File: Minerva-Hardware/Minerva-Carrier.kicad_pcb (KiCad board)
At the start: 4 copper layers, 83.5 x 90 mm, 75 parts, among them J1 HDMI_D_1.4, J11 USB_C_Receptacle_USB2.0, J14 JST_SHBM04B-SRSS-TB, J16 Conn_01x22_Female, J2 Conn_02x07_Odd_Even, J3 Bus_M.2_Socket_B, J4 Bus_M.2_Socket_M, J5 Conn_01x22_Female, J6 THD-02-R, J7 JAE_SIM_Card_SF72S006, J8 THD-20-R, SW1 Right angle Tact button, U1 BQ25798, U2 ASEK-32.768KHZ-L-R-T, U6 AP22653W6, U8 AP3441SHE-7B

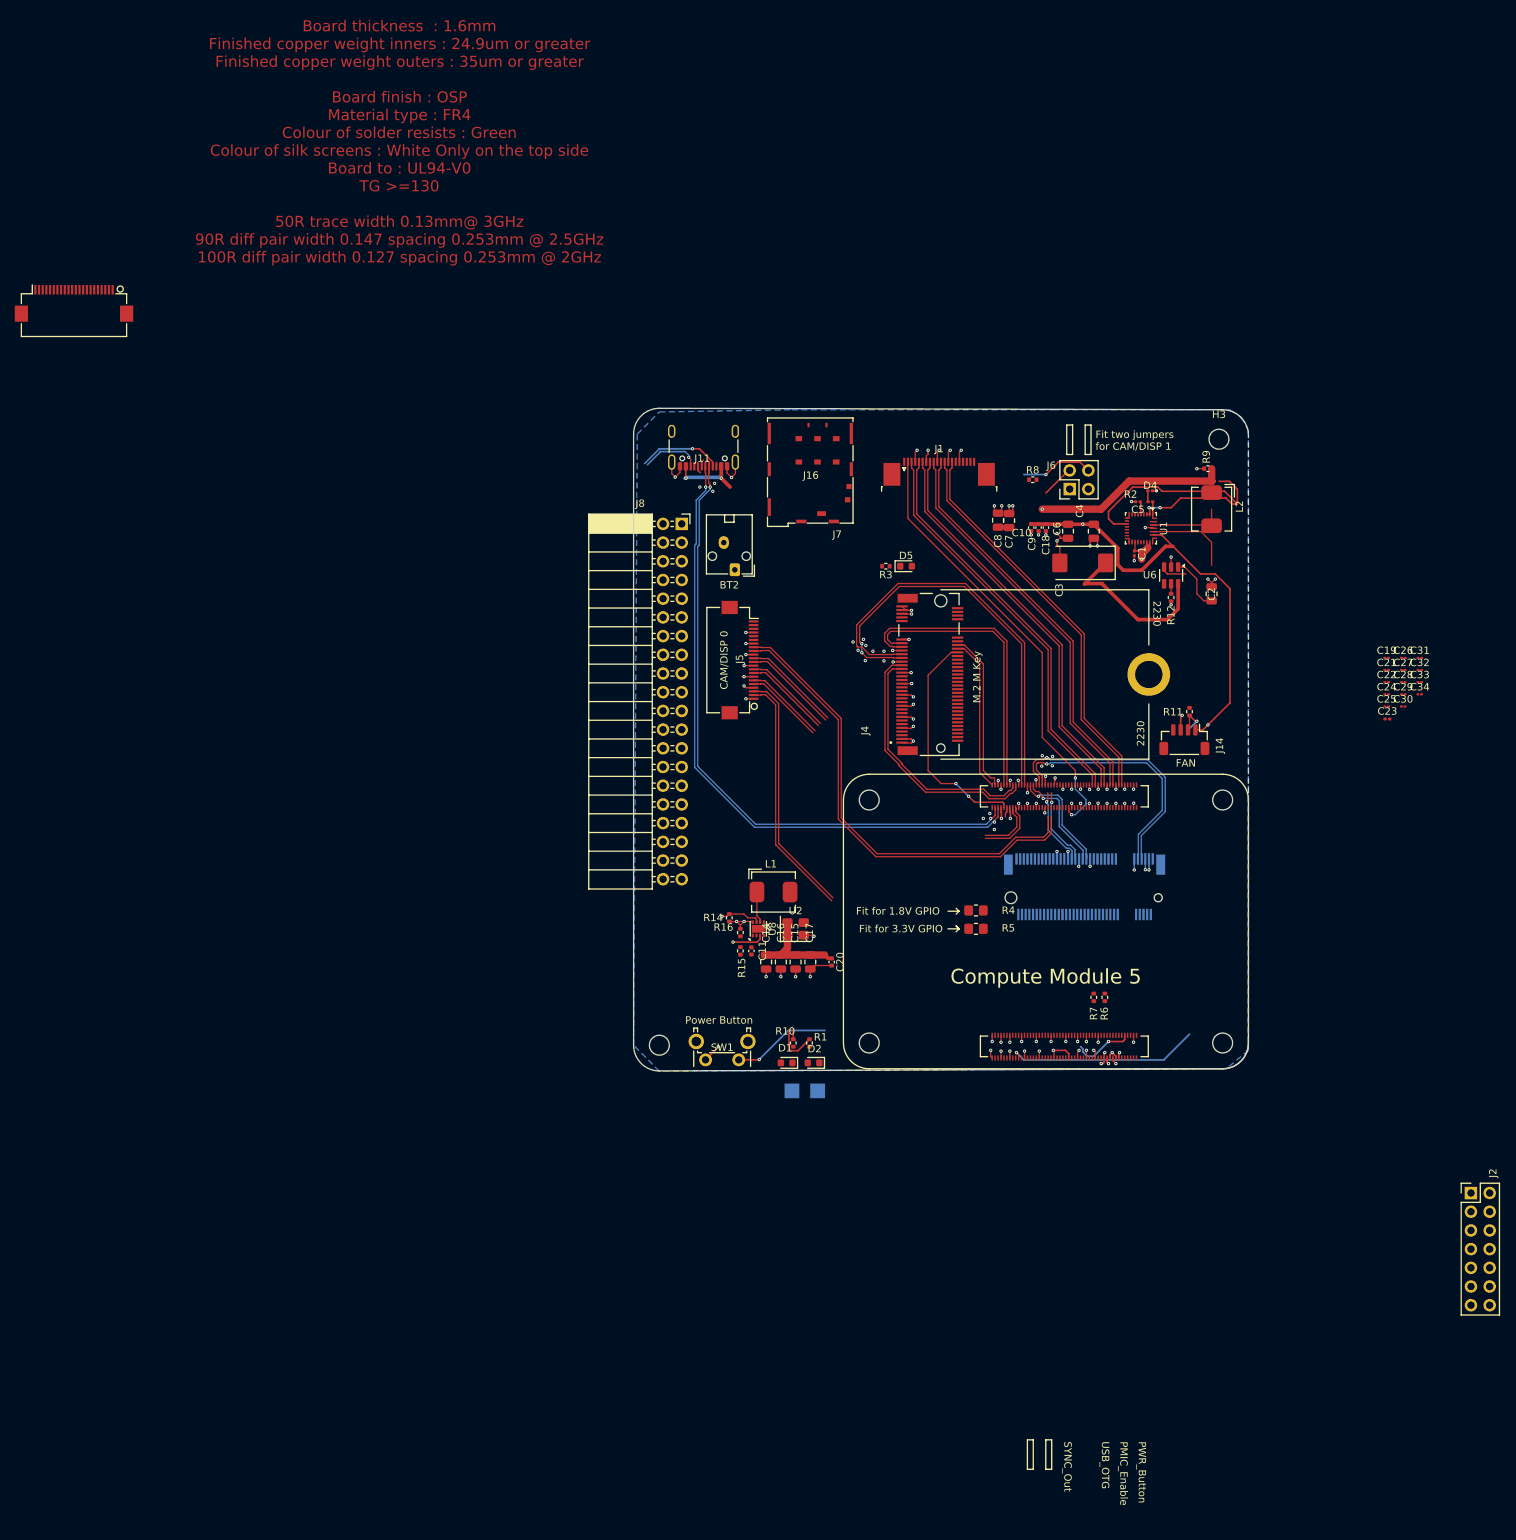
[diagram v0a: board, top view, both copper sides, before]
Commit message: Capture pre-existing Minerva hardware and Torchform work
Hardware schematics and power architecture
- Update carrier, CM5 GPIO, high-speed, PCIe/M.2, face-board, and root schematic hierarchy.
- Add USB-C/DisplayPort dock path, PD controller support, display bridge, audio amplifier, battery charging, boost conversion, fuel gauge, RTC backup, and MCU interconnect changes.
- Add the relocated power/USB schematic and associated local symbols, footprints, and 3D models.

PCB and design assets
- Update the carrier PCB and project configuration.
- Add CM5, connector, power, battery, PD, and board-specific footprint libraries.
- Add the USB-C receptacle STEP model and supporting KiCad assets.
- Apply the surfaced carrier-board geometry cleanup and add the J23 shell-peg DRC rule.

Verification and reference material
- Add CM5 and component datasheets, extracted reference text, current netlist, DRC output, and hardware verification documentation.
- Update CONTEXT.md and workspace metadata with the current project state.

Torchform companion projects
- Add the standalone Qt/QML gamepad prototype.
- Add the Torchform QML GUI shell with screen, panel, radial-menu, keyboard, status, and startup components.
- Add the companion Rust input daemon prototype and configuration.

Project notes
- Add repository guidance and Minerva design/editor notes, including the power-usage note.
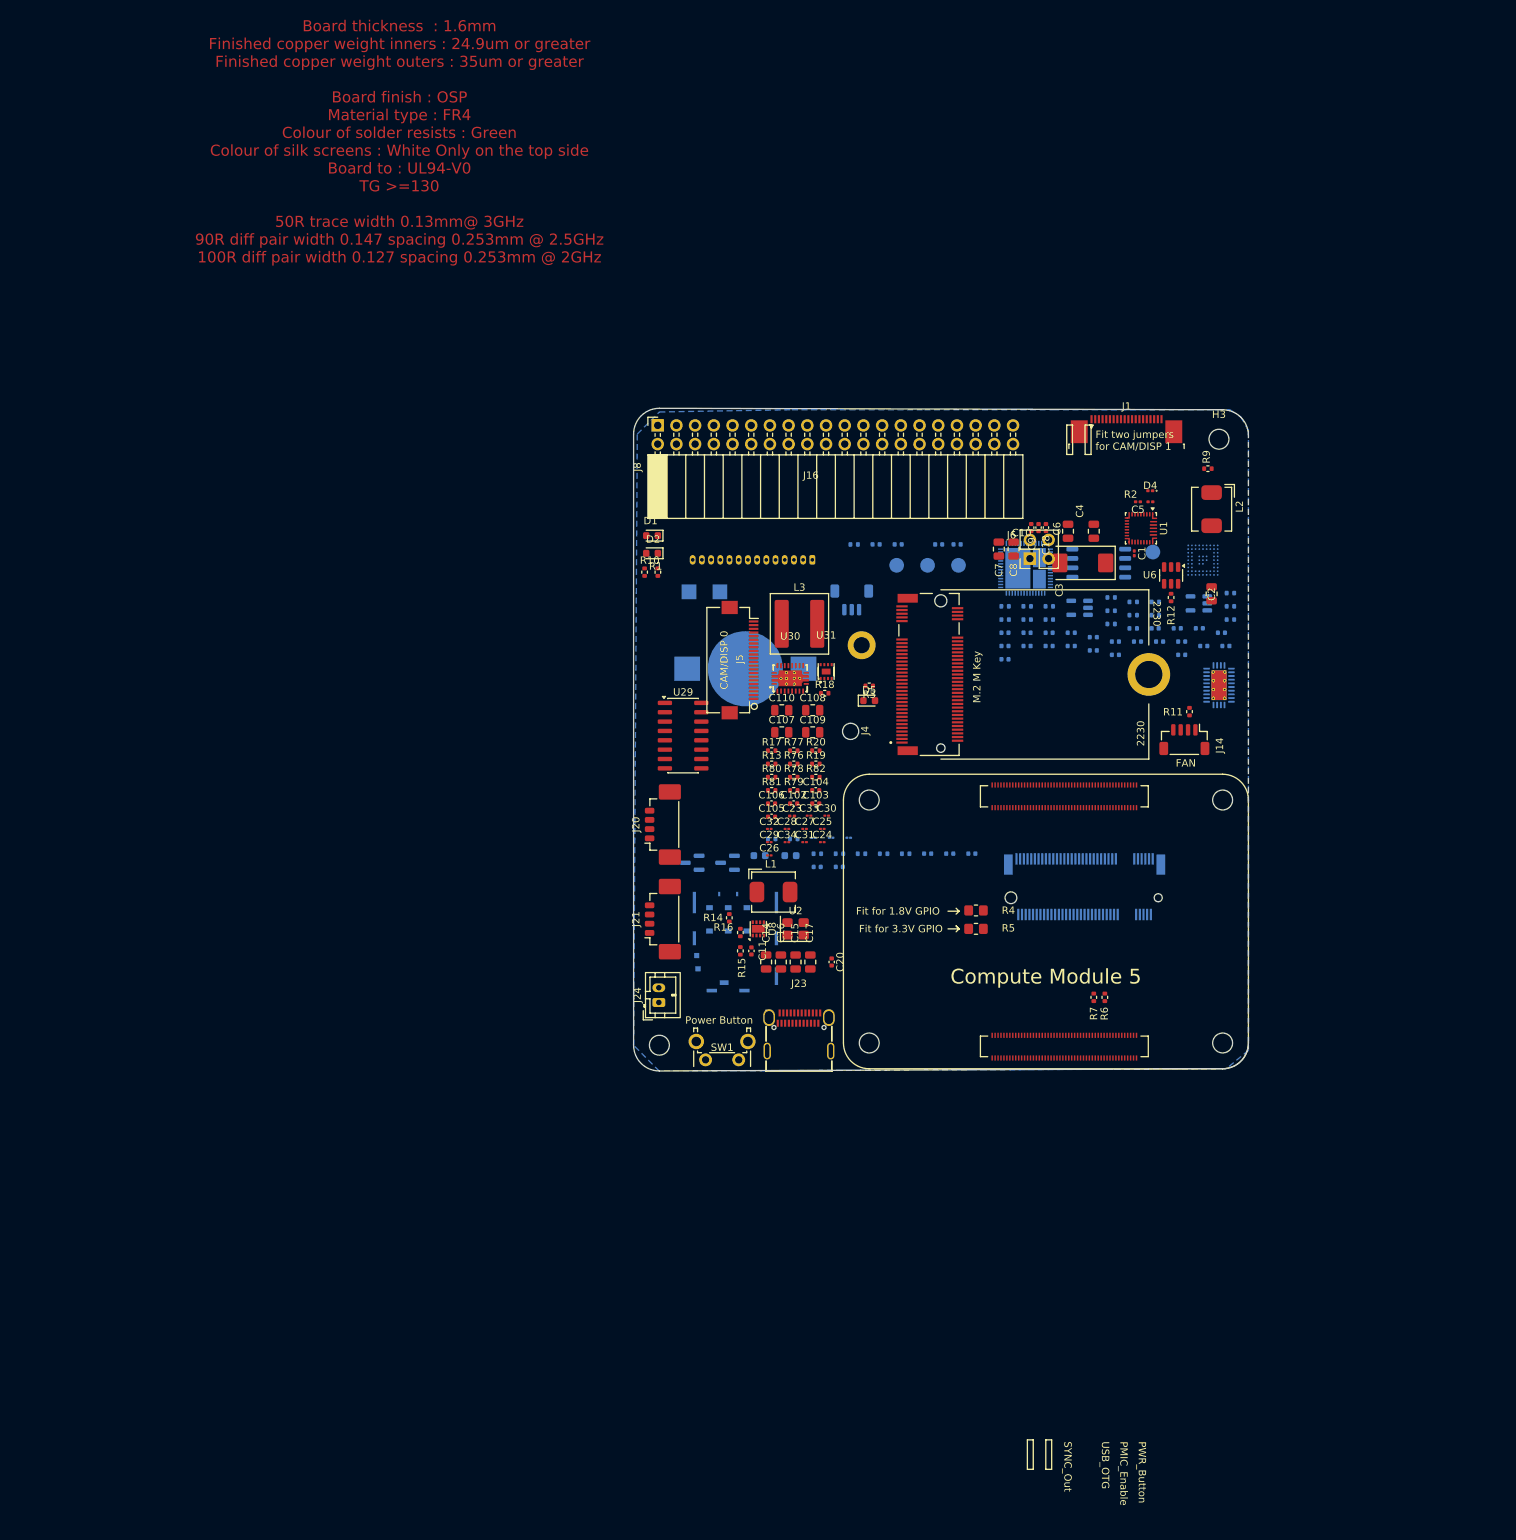
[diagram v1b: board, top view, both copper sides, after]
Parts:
- removed BT2: Battery, Connector_JST:JST_ZE_S02B-ZESK-2D_1x02_P1.50mm_Horizontal
- removed J11: USB_C_Receptacle_USB2.0, Connector_USB:USB_C_Receptacle_GCT_USB4105-xx-A_16P_TopMnt_Horizontal
- removed J16: Conn_01x22_Female, CM5IO:Hirose_FH12-22S-0.5SH_1x22-1MP_P0.50mm_Horizontal
- removed J2: Conn_02x07_Odd_Even, Connector_PinHeader_2.54mm:PinHeader_2x07_P2.54mm_Vertical
- removed R8: 2.2K 1%, Resistor_SMD:R_0402_1005Metric
- added BT3: ML1220, BatteryHolder_Keystone_3000_1x12mm, B.Cu at (94.2, 105.4)
- added C100: 1uF, C_0402_1005Metric, B.Cu at (103.9, 132.3)
- added C101: 1uF, C_0402_1005Metric, B.Cu at (118.9, 130.5)
- added C102: 100nF, C_0402_1005Metric, F.Cu at (100.7, 123.7)
- added C103: 3.3nF, C_0402_1005Metric, F.Cu at (103.7, 123.7)
- added C104: 47nF, C_0402_1005Metric, F.Cu at (103.7, 121.9)
- added C105: 1uF, C_0402_1005Metric, F.Cu at (97.7, 125.5)
- added C106: 100nF, C_0402_1005Metric, F.Cu at (97.7, 123.7)
- added C107: 22uF 10V, C_0805_2012Metric, F.Cu at (99.1, 114.0)
- added C108: 22uF 10V, C_0805_2012Metric, F.Cu at (103.3, 111.0)
- added C109: 22uF 10V, C_0805_2012Metric, F.Cu at (103.3, 114.0)
- added C110: 22uF 10V, C_0805_2012Metric, F.Cu at (99.1, 111.0)
- added C12: C, C_0402_1005Metric, B.Cu at (111.9, 88.5)
- added C13: C, C_0402_1005Metric, B.Cu at (114.9, 88.5)
- added C70: 100nF, C_0402_1005Metric, B.Cu at (129.4, 100.5)
- added C71: 100nF, C_0402_1005Metric, B.Cu at (159.4, 102.3)
- added C72: 100nF, C_0402_1005Metric, B.Cu at (144.4, 101.7)
- added C73: 100nF, C_0402_1005Metric, B.Cu at (129.4, 102.3)
- added C74: 100nF, C_0402_1005Metric, B.Cu at (120.4, 88.5)
- added C75: 10uF, C_0402_1005Metric, B.Cu at (141.4, 101.1)
- added C76: 10uF, C_0402_1005Metric, B.Cu at (138.4, 100.5)
- added C77: 1uF, C_0402_1005Metric, B.Cu at (150.4, 101.7)
- added C78: 1uF, C_0402_1005Metric, B.Cu at (122.9, 88.5)
- added C79: 1uF, C_0402_1005Metric, B.Cu at (135.4, 100.5)
- added C80: 100nF, C_0402_1005Metric, B.Cu at (149.8, 99.9)
- added C81: 100nF, C_0402_1005Metric, B.Cu at (135.4, 102.3)
- added C82: 10uF, C_0402_1005Metric, B.Cu at (144.4, 103.5)
- added C83: 10uF, C_0402_1005Metric, B.Cu at (141.4, 102.9)
- added C84: 1uF, C_0402_1005Metric, B.Cu at (129.4, 104.1)
- added C85: 1uF, C_0402_1005Metric, B.Cu at (153.4, 103.5)
- added C86: 390pF, C_0402_1005Metric, B.Cu at (132.4, 100.5)
- added C87: 390pF, C_0402_1005Metric, B.Cu at (156.4, 102.3)
- added C88: 100nF, C_0402_1005Metric, B.Cu at (147.4, 101.7)
- added C89: 100nF, C_0402_1005Metric, B.Cu at (153.4, 101.7)
- added C90: 1uF, C_0402_1005Metric, B.Cu at (152.8, 99.9)
- added C91: 100nF, C_0402_1005Metric, B.Cu at (138.4, 102.3)
- added C92: 100nF, C_0402_1005Metric, B.Cu at (155.8, 99.9)
- added C93: 100nF, C_0402_1005Metric, B.Cu at (132.4, 102.3)
- added C94: 100nF, C_0402_1005Metric, B.Cu at (158.8, 100.5)
- added C95: 100nF, C_0402_1005Metric, B.Cu at (124.9, 130.5)
- added C96: 10uF, C_0603_1608Metric, B.Cu at (96.1, 130.8)
- added C97: 100nF, C_0402_1005Metric, B.Cu at (106.9, 132.3)
- added C98: 10uF, C_0603_1608Metric, B.Cu at (100.3, 130.8)
- added C99: 1uF, C_0402_1005Metric, B.Cu at (121.9, 130.5)
- added D6: BAT54, D_SOT-23_BAT54_AK, B.Cu at (87.0, 131.7)
- added D7: BAT54, D_SOT-23_BAT54_AK, B.Cu at (91.8, 131.7)
- added J20: SPK_1.25mm_4P, Molex_PicoBlade_53398-0471_1x04-1MP_P1.25mm_Vertical, F.Cu at (82.4, 126.5)
- added J21: SPK_1.25mm_4P, Molex_PicoBlade_53398-0471_1x04-1MP_P1.25mm_Vertical, F.Cu at (82.4, 139.4)
- added J22: AUX_IN_3.5mm, JST_SH_BM03B-SRSS-TB_1x03-1MP_P1.00mm_Vertical, B.Cu at (108.6, 96.0)
- added J23: USB-C 24P (C5156605), USBC_24P_QT143, F.Cu at (101.5, 154.7)
- added J24: BATT JST-PH 2P, JST_PH_B2B-PH-K_1x02_P2.00mm_Vertical, F.Cu at (82.4, 150.7)
- added J25: FACEPLATE 14P, Molex_PicoBlade_53047-1410_1x14_P1.25mm_Vertical, B.Cu at (103.3, 90.6)
- added L3: 1.8uH XAL7070-182ME, L_Coilcraft_XAL7070-XXX, F.Cu at (101.5, 99.3)
- added M6: M.2 Solder Nut, MountingHole_2.2mm_M2_DIN965_Pad, B.Cu at (110.0, 102.2)
- added M7: M.2 Screw, MountingHole_2.2mm_M2, B.Cu at (108.5, 113.9)
- added R13: 100Ω, R_0402_1005Metric, F.Cu at (97.8, 118.3)
- added R17: 3kΩ, R_0402_1005Metric, F.Cu at (97.8, 116.5)
- added R18: 30.1kΩ, R_0402_1005Metric, F.Cu at (105.0, 108.7)
- added R19: 10kΩ, R_0402_1005Metric, F.Cu at (103.8, 118.3)
- added R20: 10kΩ, R_0402_1005Metric, F.Cu at (103.8, 116.5)
- added R50: 51K 1%, R_0402_1005Metric, B.Cu at (146.9, 98.1)
- added R51: 10K, R_0402_1005Metric, B.Cu at (149.9, 98.1)
- added R52: 10K, R_0402_1005Metric, B.Cu at (160.1, 98.7)
- added R53: 10K, R_0402_1005Metric, B.Cu at (146.9, 99.9)
- added R54: 10K, R_0402_1005Metric, B.Cu at (132.5, 98.7)
- added R55: 10K, R_0402_1005Metric, B.Cu at (160.1, 96.9)
- added R56: 10K, R_0402_1005Metric, B.Cu at (132.5, 96.9)
- added R57: 100K, R_0402_1005Metric, B.Cu at (143.9, 95.7)
- added R58: 1M, R_0402_1005Metric, B.Cu at (160.1, 95.1)
- added R59: 10K, R_0402_1005Metric, B.Cu at (129.5, 96.9)
- added R60: 10K, R_0402_1005Metric, B.Cu at (149.9, 96.3)
- added R61: 10K, R_0402_1005Metric, B.Cu at (146.9, 96.3)
- added R62: 10K, R_0402_1005Metric, B.Cu at (129.5, 98.7)
- added R63: 100K, R_0402_1005Metric, B.Cu at (135.5, 96.9)
- added R64: 100K, R_0402_1005Metric, B.Cu at (143.9, 97.5)
- added R65: 100K, R_0402_1005Metric, B.Cu at (143.9, 99.3)
- added R66: 100K, R_0402_1005Metric, B.Cu at (135.5, 98.7)
- added R71: 100K, R_0402_1005Metric, B.Cu at (116.0, 130.5)
- added R72: 100K, R_0402_1005Metric, B.Cu at (110.0, 130.5)
- added R73: 0R (DNP option), R_0402_1005Metric, B.Cu at (100.8, 128.5)
- added R74: 0R (DNP option), R_0402_1005Metric, B.Cu at (97.8, 128.5)
- added R75: 1kΩ, R_0402_1005Metric, B.Cu at (107.0, 130.5)
- added R76: 5.23kΩ, R_0402_1005Metric, F.Cu at (100.8, 118.3)
- added R77: 10kΩ, R_0402_1005Metric, F.Cu at (100.8, 116.5)
- added R78: 182kΩ 1%, R_0402_1005Metric, F.Cu at (100.8, 120.1)
- added R79: 56kΩ 1%, R_0402_1005Metric, F.Cu at (100.8, 121.9)
- added R80: 8.2kΩ, R_0402_1005Metric, F.Cu at (97.8, 120.1)
- added R81: 64.9kΩ 1%, R_0402_1005Metric, F.Cu at (97.8, 121.9)
- added R82: 100kΩ 1%, R_0402_1005Metric, F.Cu at (103.8, 120.1)
- added R84: 100kΩ, R_0402_1005Metric, B.Cu at (109.0, 88.5)
- added R85: 2.2kΩ, R_0402_1005Metric, B.Cu at (113.0, 130.5)
- added R86: 2.2kΩ, R_0402_1005Metric, B.Cu at (104.0, 130.5)
- added TP10: +5v PAD, TestPoint_Pad_D2.0mm, B.Cu at (149.5, 89.5)
- added TP11: +5v PAD, TestPoint_Pad_D2.0mm, B.Cu at (114.7, 91.3)
- added TP12: GND PAD, TestPoint_Pad_D2.0mm, B.Cu at (118.9, 91.3)
- added TP13: GND PAD, TestPoint_Pad_D2.0mm, B.Cu at (123.1, 91.3)
- added U20: SN65DSI86ZQER, nFBGA-64_ZQE_5x5mm_P0.5mm, B.Cu at (156.3, 90.6)
- added U21: HD3SS460RHRT, WQFN-28-1EP_3.5x5.5mm_P0.5mm_EP2.05x4.05mm_ThermalVias, B.Cu at (158.5, 107.6)
- added U22: TPS65987DDJRSHR, TPS65987D_VQFN56_RSH, B.Cu at (132.2, 91.7)
- added U23: W25Q32JVSS, SOIC-8_5.3x5.3mm_P1.27mm, B.Cu at (142.2, 91.0)
- added U24: AP2112K-1.8, SOT-23-5, B.Cu at (155.8, 96.5)
- added U25: AP2112K-1.2, SOT-23-5, B.Cu at (139.6, 97.1)
- added U29: PAM8406DR, SOIC-16_3.9x9.9mm_P1.27mm, F.Cu at (85.7, 114.5)
- added U30: TPS61088RHLR, VQFN-20-1EP_3.5x4.5mm_P0.5mm_EP2.15x3.15mm, F.Cu at (100.3, 106.7)
- added U31: MAX17048G+T10, MAX17048_TDFN8, F.Cu at (105.2, 105.8)
- C19, C21, C22, J7: moved to B.Cu
- H2, H3: footprint CM5IO:MountingHole_2.7mm_M2.5_DIN965 -> MountingHole:MountingHole_2.7mm_M2.5_DIN965
- J5: footprint CM5IO:Hirose_FH12-22S-0.5SH_1x22-1MP_P0.50mm_Horizontal -> Connector_FFC-FPC:Hirose_FH12-22S-0.5SH_1x22-1MP_P0.50mm_Horizontal
- L1: footprint CM5IO:L_Bourns_SRP5030CC -> Inductor_SMD:L_Bourns_SRP5030T
- L2: footprint CM5 IO Board-rev2:L_Bourns_SRP5030CC -> Inductor_SMD:L_Bourns_SRP5030T
- moved C32 90.9 mm to (97.4, 127.1)
- moved C26 90.2 mm to (97.4, 130.7)
- moved C29 88.4 mm to (97.4, 128.9)
- moved C34 88.3 mm to (99.8, 128.9)
- moved C31 87.2 mm to (102.2, 128.9)
- moved C28 86.0 mm to (99.8, 127.1)
- moved C33 84.9 mm to (102.8, 125.3)
- moved C27 84.1 mm to (102.2, 127.1)
- moved C23 81.9 mm to (100.5, 125.4)
- moved C22 80.7 mm to (103.4, 128.3), turned to 180 degrees
- moved C30 79.7 mm to (105.2, 125.3)
- moved C24 79.2 mm to (104.6, 128.9)
- moved C21 78.8 mm to (105.8, 128.3), turned to 180 degrees
- moved C25 78.4 mm to (104.6, 127.1)
- moved C19 77.0 mm to (108.2, 128.3), turned to 180 degrees
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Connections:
- net /BATP renamed /Power and UserIO/BATP
- net /BTST1 renamed /Power and UserIO/BTST1
- net /BTST2 renamed /Power and UserIO/BTST2
- net /CM5_GPIO/GPIO2 renamed /CM5_GPIO/SDA_I2C
- net /CM5_GPIO/GPIO26 renamed /DSI86_EN
- net /CM5_GPIO/GPIO3 renamed /CM5_GPIO/SCL_I2C
- net /CM5_HighSpeed/USB3-0-D_N renamed /CM5_HighSpeed/USB-3_N
- net /CM5_HighSpeed/USB3-0-D_P renamed /CM5_HighSpeed/USB-3_P
- net /REGN renamed /Power and UserIO/REGN
- net /SW1 renamed /Power and UserIO/SW1
- net /SW2 renamed /Power and UserIO/SW2
- net /SYS_OUT renamed /Power and UserIO/SYS_OUT
- C19 pad 1: /VBUS -> Net-(C19-Pad1)
- C2 pad 1: /CM5_HighSpeed/+5v -> /+5v
- C21 pad 1: /VBUS -> Net-(C19-Pad1)
- C22 pad 1: /VBUS -> Net-(C19-Pad1)
- C3 pad 1: /CM5_HighSpeed/VBUS -> /VBUS
- C7 pad 1: /CM5_HighSpeed/VBUS -> /VBUS
- C8 pad 1: /CM5_HighSpeed/VBUS -> /VBUS
- D1 pad 2: /CM5_GPIO/+3.3v -> +3.3v
- D2 pad 2: /CM5_GPIO/+3.3v -> +3.3v
- D4 pad 1: GND -> /Power and UserIO/CRG_IND_SIG
- J1 pad 19: /CM5_HighSpeed/+5v -> /+5v
- J1 pad 20: (no net) -> GND
- J1 pad MP: (no net) -> GND
- J3 pad 50: /PCIe-M2/PERST -> /PCIE_nRST
- J3 pad 6: unconnected-(J3-~{FULL_CARD_POWER_OFF}-Pad6) -> /PCIe-M2/M2_FCPO
- J3 pad 76: (no net) -> GND
- J3 pad 77: (no net) -> GND
- J4 pad 50: /CM5_HighSpeed/PCIE_nRST -> /PCIE_nRST
- J5 pad 22: /+3.3v -> +3.3v
- J8 pad 1: /CM5_GPIO/+3.3v -> +3.3v
- J8 pad 17: /CM5_GPIO/+3.3v -> +3.3v
- Module1 pad 109: /CM5_HighSpeed/PCIE_nRST -> /PCIE_nRST
- Module1 pad 157: GND -> /CM5_HighSpeed/USB3-1-RX_N
- Module1 pad 159: GND -> /CM5_HighSpeed/USB3-1-RX_P
- Module1 pad 163: GND -> /CM5_HighSpeed/USB3-1-D_P
- Module1 pad 165: GND -> /CM5_HighSpeed/USB3-1-D_N
- Module1 pad 169: GND -> /CM5_HighSpeed/USB3-1-TX_N
- Module1 pad 171: GND -> /CM5_HighSpeed/USB3-1-TX_P
- Module1 pad 84: /CM5_GPIO/+3.3v -> +3.3v
- Module1 pad 86: /CM5_GPIO/+3.3v -> +3.3v
- Module1 pad 94: /CC1 -> /CM5_CC1
- Module1 pad 96: /CC2 -> /CM5_CC2
- Module1 pad 99: /CM5_GPIO/PMIC_ENABLE -> unconnected-(Module1A-PMIC_ENABLE-Pad99)
- R11 pad 1: /CM5_GPIO/+3.3v -> +3.3v
- R2 pad 1: +3.3V -> +3.3v
- R5 pad 1: /CM5_GPIO/+3.3v -> +3.3v
- U1 pad 1: +3.3V -> /Power and UserIO/CRG_IND_SIG
- U1 pad 16: Net-(U1-TS) -> /Power and UserIO/TS
- U6 pad 1: /CM5_HighSpeed/+5v -> /+5v
- U6 pad 6: /CM5_HighSpeed/VBUS -> /VBUS
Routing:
- net /+5v: track 274.1 -> 0.00 mm, vias 9 -> 0
- net GND: track 144.3 -> 0.00 mm, vias 131 -> 0
- net (no net): track 134.8 -> 0.00 mm, vias 1 -> 0
- net /USB2_P: track 89.9 -> 0.00 mm, vias 2 -> 0
- net /USB2_N: track 89.7 -> 0.00 mm, vias 2 -> 0
- net /CM5_HighSpeed/DPHY0_D3_N: track 63.6 -> 0.00 mm
- net /CM5_HighSpeed/DPHY0_D3_P: track 62.9 -> 0.00 mm
- net /CM5_HighSpeed/HDMI_0_HOTPLUG: track 60.2 -> 0.00 mm, vias 2 -> 0
- net /CM5_HighSpeed/PCIE_TX_N: track 57.3 -> 0.00 mm
- net /CM5_HighSpeed/PCIE_TX_P: track 56.1 -> 0.00 mm, vias 2 -> 0
- net /CM5_HighSpeed/HDMI_D2_P: track 54.1 -> 0.00 mm
- net /CM5_HighSpeed/HDMI_D2_N: track 54.1 -> 0.00 mm
- net /CM5_HighSpeed/HDMI_D1_P: track 53.9 -> 0.00 mm
- net /CM5_HighSpeed/HDMI_D1_N: track 53.9 -> 0.00 mm
- net /CM5_HighSpeed/HDMI_D0_N: track 53.8 -> 0.00 mm
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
